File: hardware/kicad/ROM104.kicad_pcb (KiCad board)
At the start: 2 copper layers, 75 x 75 mm, 30 parts, among them J1 Screw_Terminal_01x12, J2 CAN, K1 DIPxx-1Cxx-51x, K2 DIPxx-1Cxx-51x, K3 DIPxx-1Cxx-51x, K4 DIPxx-1Cxx-51x, SW1 INSTANCE, SW2 BUS, U1 L293D, U2 MCP2551-I-P, U3 TMR_2411, U4 Teensy_3.2, U5 L293D

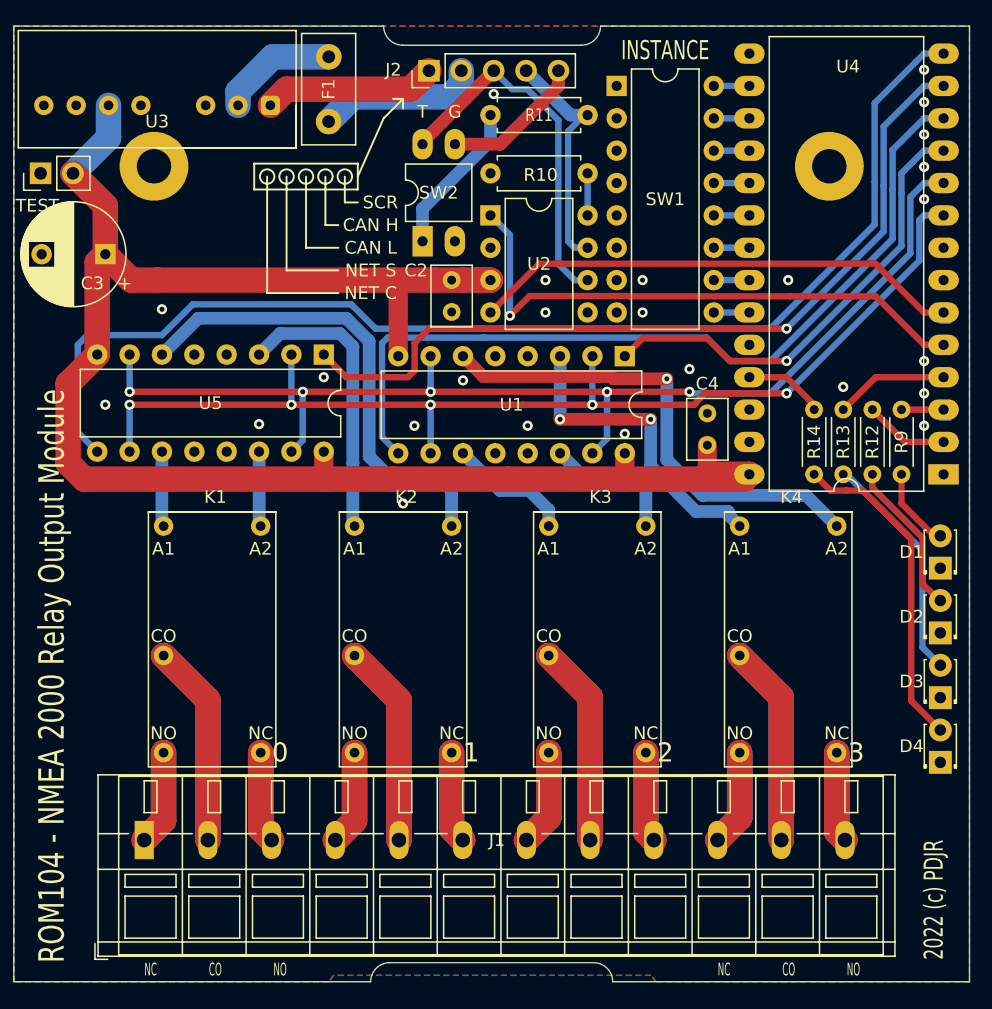
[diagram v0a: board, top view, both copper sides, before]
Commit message: Change relay terminal
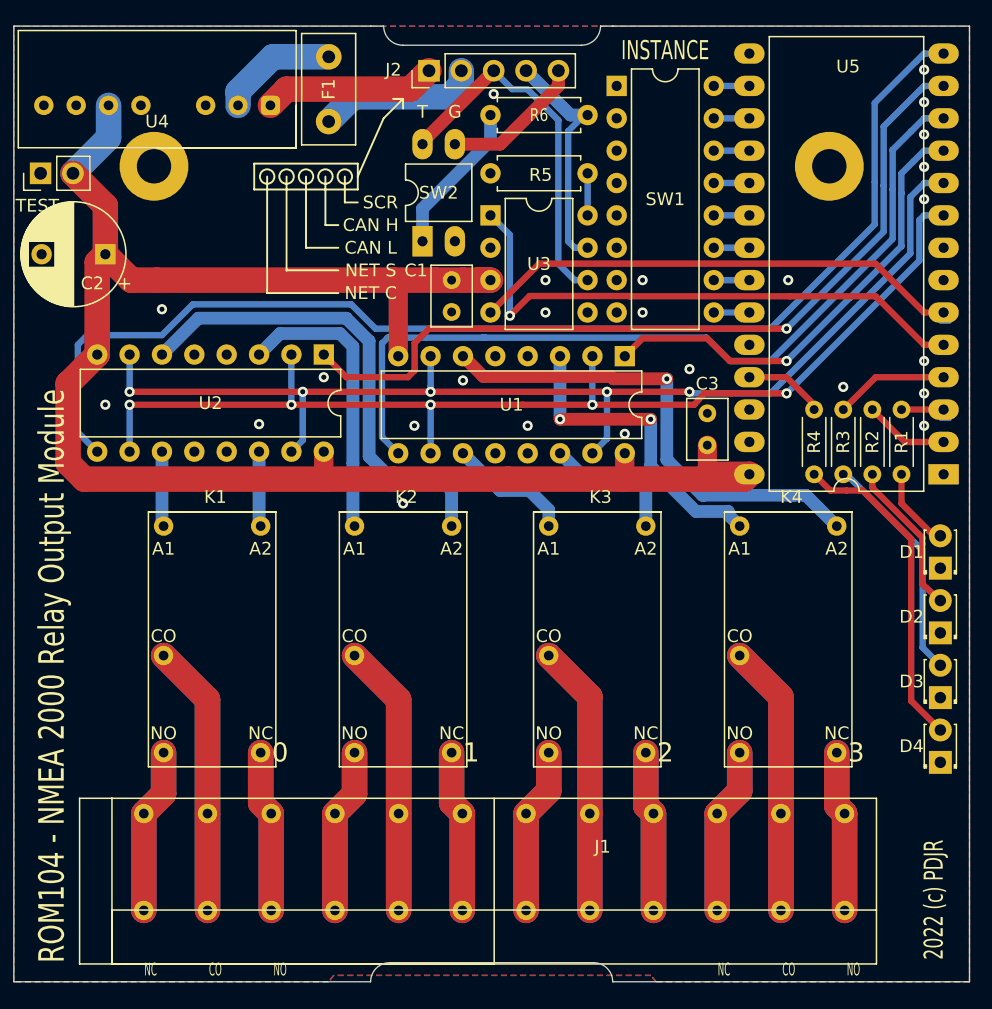
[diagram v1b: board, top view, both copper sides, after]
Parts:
- J1: footprint TerminalBlock_WAGO:TerminalBlock_WAGO_236-112_1x12_P5.00mm_45Degree -> PDJR-connectors:WURTH-401B-12PIN
- moved J1 5.52 mm to (146.2, 156.4)
- renumbered C2 to C1, C3 to C2, C4 to C3, R9 to R1, R12 to R2, R13 to R3, R14 to R4, R10 to R5, R11 to R6, U5 to U2, U2 to U3, U3 to U4, U4 to U5
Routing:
- net Net-(J1-Pad10): track 15.2 -> 26.2 mm
- net Net-(J1-Pad7): track 15.2 -> 26.2 mm
- net Net-(J1-Pad4): track 15.0 -> 26.0 mm
- net Net-(J1-Pad1): track 15.0 -> 26.0 mm
- net Net-(J1-Pad11): track 31.7 -> 42.7 mm
- net Net-(J1-Pad9): track 14.2 -> 25.3 mm
- net Net-(J1-Pad12): track 14.2 -> 25.3 mm
- net Net-(J1-Pad6): track 14.4 -> 25.5 mm
- net Net-(J1-Pad3): track 14.4 -> 25.4 mm
- net Net-(J1-Pad8): track 31.6 -> 42.7 mm
- net Net-(J1-Pad5): track 31.8 -> 42.9 mm
- net Net-(J1-Pad2): track 31.8 -> 42.9 mm

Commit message: PCB tweak
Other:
- board text removed: "0"
- board text removed: "1"
- board text removed: "2"
- board text removed: "3"
- board text removed: "CAN H"
- board text removed: "CAN L"
- board text removed: "NET C"
- board text removed: "NET S"
- board text removed: "SCR"

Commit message: Change resistor footprints
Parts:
- R5: footprint Resistor_THT:R_Axial_DIN0207_L6.3mm_D2.5mm_P7.62mm_Horizontal -> Resistor_THT:R_Axial_DIN0204_L3.6mm_D1.6mm_P5.08mm_Horizontal
- moved D1 4.07 mm to (209.0, 125.5), turned to 270 degrees
- moved D2 4.07 mm to (209.0, 130.6), turned to 270 degrees
- moved D3 4.07 mm to (209.0, 135.6), turned to 270 degrees
- moved D4 4.07 mm to (209.0, 140.7), turned to 270 degrees
- moved R5 2.59 mm to (175.9, 99.1)
- moved R4 1.27 mm to (197.5, 117.1)
- moved R3 1.02 mm to (200.1, 117.1)
- moved R2 0.76 mm to (202.6, 117.1)
- moved R1 0.51 mm to (205.2, 117.1)
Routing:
- net Net-(D3-Pad2): track 18.3 -> 20.4 mm
- net Net-(D1-Pad2): track 6.39 -> 8.31 mm
- net Net-(D2-Pad2): track 12.2 -> 14.1 mm
- net Net-(D4-Pad2): track 25.7 -> 27.5 mm
- net /CH2_LED: track 8.93 -> 10.0 mm
- net /CAN_H: track 18.5 -> 17.8 mm
- net /CH1_LED: track 6.64 -> 7.30 mm
- net /CAN_L: track 28.9 -> 28.3 mm
- net Net-(R5-Pad2): track 3.30 -> 2.79 mm
- net GND: vias 25 -> 26

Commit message: Update PCB
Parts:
- removed R1, R2, R3, R4: 470R, Resistor_THT:R_Axial_DIN0204_L3.6mm_D1.6mm_P5.08mm_Horizontal
- added RN1: 470R, Resistor_THT:R_Array_SIP5, F.Cu at (209.0, 146.3)
- K1, K2, K3, K4: value DIPxx-1Cxx-51x -> SPDT_RELAY
- R5: footprint Resistor_THT:R_Axial_DIN0204_L3.6mm_D1.6mm_P5.08mm_Horizontal -> Resistor_THT:R_Axial_DIN0207_L6.3mm_D2.5mm_P7.62mm_Horizontal
- moved R5 2.59 mm to (173.4, 98.6)
- moved D1 2.54 mm to (209.0, 128.0), turned to 90 degrees
- moved D2 2.54 mm to (209.0, 133.1), turned to 90 degrees
- moved D3 2.54 mm to (209.0, 138.2), turned to 90 degrees
- moved D4 2.54 mm to (209.0, 143.3), turned to 90 degrees
- moved K4 2.38 mm to (192.3, 146.3)
- moved K3 2.35 mm to (177.4, 146.3)
- moved K1 2.33 mm to (147.3, 146.3)
- moved K2 2.31 mm to (162.4, 146.3)
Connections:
- D1 pad 1: GND -> Net-(D1-Pad1)
- D1 pad 2: Net-(D1-Pad2) -> /CH0_LED
- D2 pad 1: GND -> Net-(D2-Pad1)
- D2 pad 2: Net-(D2-Pad2) -> /CH1_LED
- D3 pad 1: GND -> Net-(D3-Pad1)
- D3 pad 2: Net-(D3-Pad2) -> /CH2_LED
- D4 pad 1: GND -> Net-(D4-Pad1)
- D4 pad 2: Net-(D4-Pad2) -> /CH3_LED
- U5 pad 2: /CH1_LED -> /CH0_LED
- U5 pad 3: /CH0_LED -> /CH1_LED
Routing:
- net /CH3_LED: track 6.46 -> 38.0 mm
- net Net-(D1-Pad1): track 0.00 -> 31.2 mm
- net Net-(D4-Pad2): track 27.5 -> 0.00 mm
- net Net-(D2-Pad1): track 0.00 -> 23.0 mm
- net Net-(D3-Pad2): track 20.4 -> 0.00 mm
- net Net-(D3-Pad1): track 0.00 -> 14.8 mm
- net Net-(D2-Pad2): track 14.1 -> 0.00 mm
- net /CH2_LED: track 10.0 -> 23.6 mm
- net Net-(D1-Pad2): track 8.31 -> 0.00 mm
- net /CH1_LED: track 7.30 -> 15.4 mm
- net Net-(D4-Pad1): track 0.00 -> 6.64 mm
- net Net-(J1-Pad7): track 26.2 -> 21.3 mm
- net Net-(J1-Pad10): track 26.2 -> 21.3 mm
- net Net-(J1-Pad1): track 26.0 -> 21.2 mm
- net Net-(J1-Pad4): track 26.0 -> 21.3 mm
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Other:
- board text removed: "CO"
- board text removed: "NC"
- board text removed: "NO"

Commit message: PCB tweak
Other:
- board text added: "CHANNEL 0"
- board text added: "CHANNEL 1"
- board text added: "CHANNEL 2"
- board text added: "CHANNEL 3"

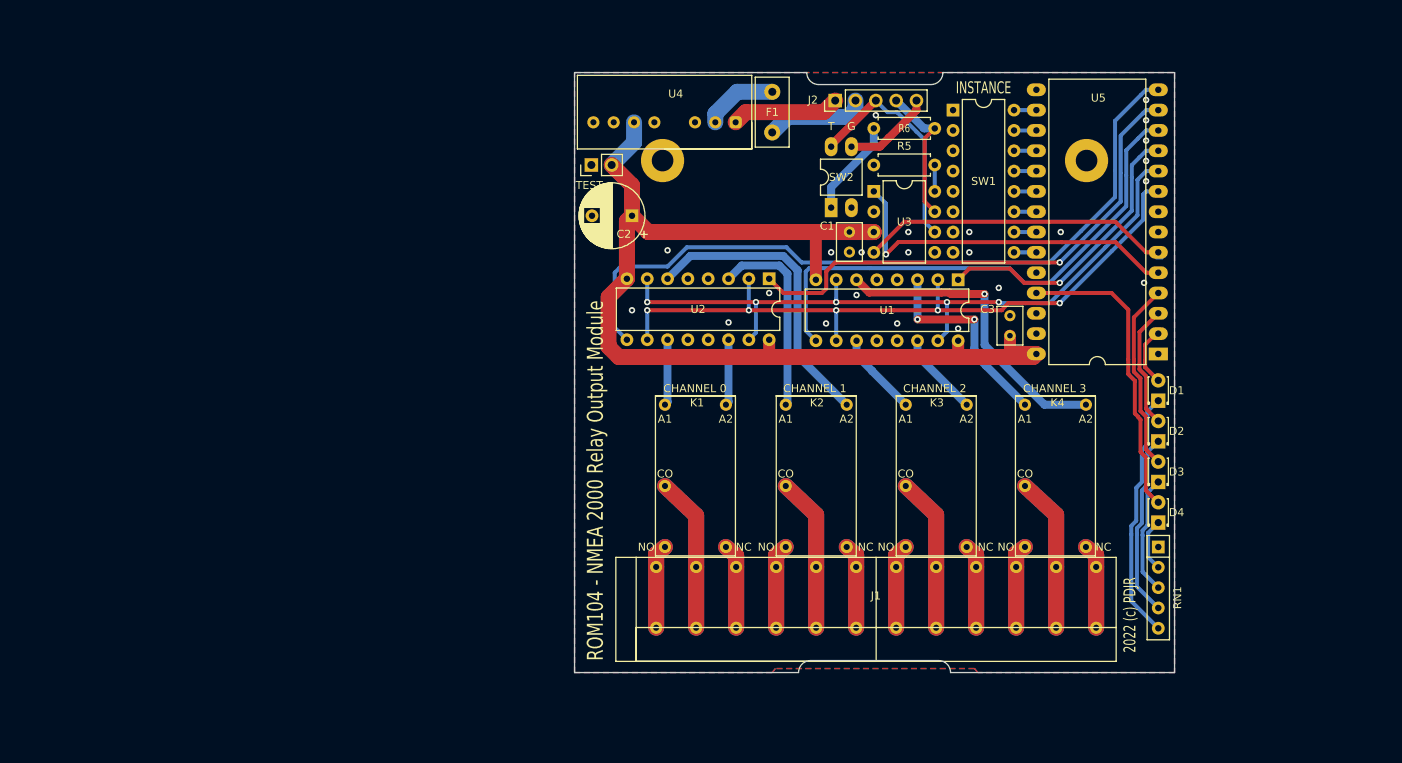
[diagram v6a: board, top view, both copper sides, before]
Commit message: PCB resize
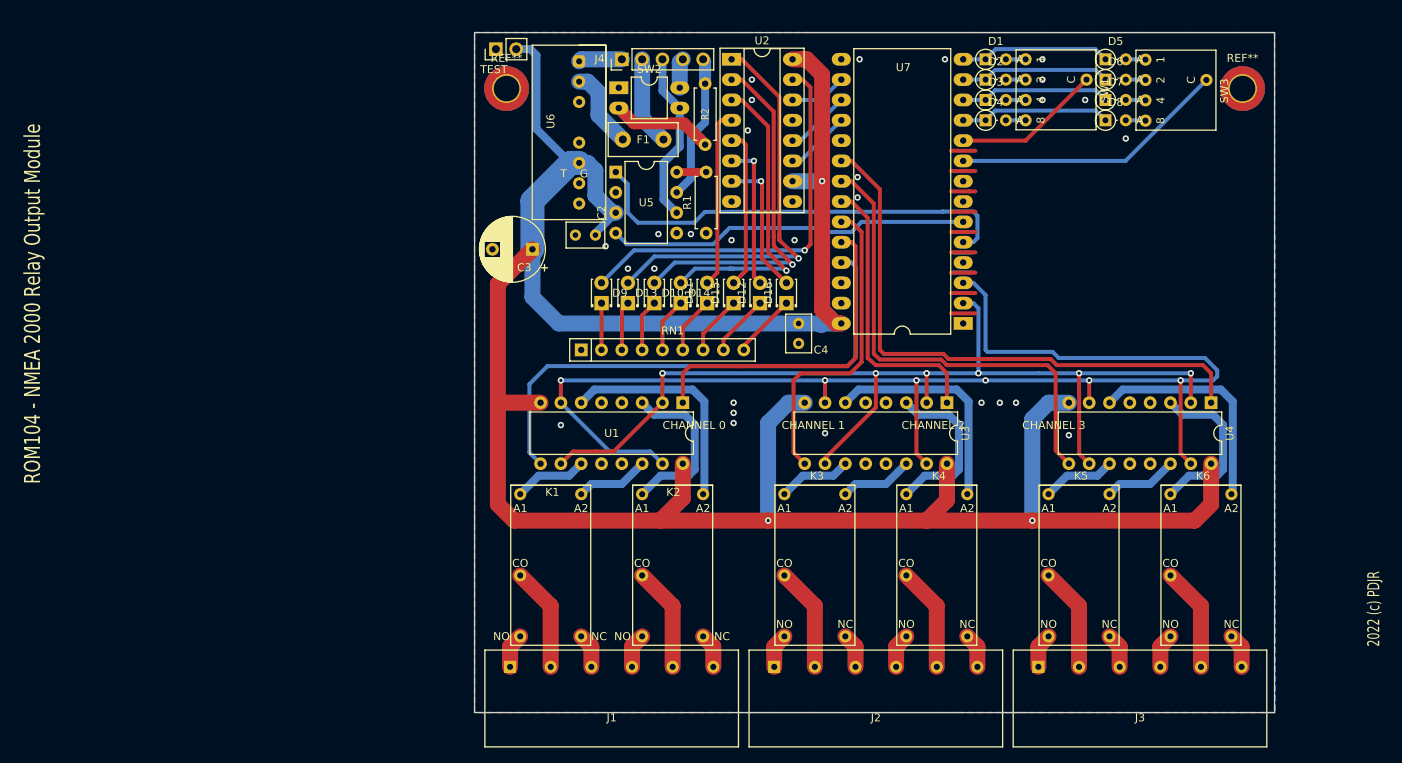
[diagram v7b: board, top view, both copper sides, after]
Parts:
- removed C1: 100n, Capacitor_THT:C_Rect_L4.6mm_W3.0mm_P2.50mm_MKS02_FKP02
- removed R5: 4K7, Resistor_THT:R_Axial_DIN0207_L6.3mm_D2.5mm_P7.62mm_Horizontal
- removed R6: 120R, Resistor_THT:R_Axial_DIN0207_L6.3mm_D2.5mm_P7.62mm_Horizontal
- removed the REF** at (200.0, 98.0)
- removed the REF** at (147.0, 98.0)
- removed the U1 at (183.9, 112.9)
- added C2: 100n, Capacitor_THT:C_Rect_L4.6mm_W3.0mm_P2.50mm_MKS02_FKP02, F.Cu at (138.6, 107.3)
- added D11: LED, LED_THT:LED_D1.8mm_W3.3mm_H2.4mm, F.Cu at (152.6, 115.8)
- added D12: LED, LED_THT:LED_D1.8mm_W3.3mm_H2.4mm, F.Cu at (159.2, 115.8)
- added D13: LED, LED_THT:LED_D1.8mm_W3.3mm_H2.4mm, F.Cu at (142.7, 115.8)
- added D15: LED, LED_THT:LED_D1.8mm_W3.3mm_H2.4mm, F.Cu at (155.9, 115.8)
- added D16: LED, LED_THT:LED_D1.8mm_W3.3mm_H2.4mm, F.Cu at (162.5, 115.8)
- added D3: D_Small, Diode_THT:D_DO-34_SOD68_P2.54mm_Vertical_AnodeUp, F.Cu at (187.4, 90.4)
- added D4: D_Small, Diode_THT:D_DO-34_SOD68_P2.54mm_Vertical_AnodeUp, F.Cu at (187.4, 93.0)
- added D5: D_Small, Diode_THT:D_DO-34_SOD68_P2.54mm_Vertical_AnodeUp, F.Cu at (202.4, 85.3)
- added D6: D_Small, Diode_THT:D_DO-34_SOD68_P2.54mm_Vertical_AnodeUp, F.Cu at (202.4, 87.9)
- added D7: D_Small, Diode_THT:D_DO-34_SOD68_P2.54mm_Vertical_AnodeUp, F.Cu at (202.4, 90.4)
- added D8: D_Small, Diode_THT:D_DO-34_SOD68_P2.54mm_Vertical_AnodeUp, F.Cu at (202.4, 93.0)
- added D9: LED, LED_THT:LED_D1.8mm_W3.3mm_H2.4mm, F.Cu at (139.4, 115.8)
- added J3: Screw_Terminal_01x06, PDJR-connectors:879-1272_TERMINAL_HEADER_6-POLE, F.Cu at (219.4, 161.3)
- added J4: CAN, Connector_PinHeader_2.54mm:PinHeader_1x05_P2.54mm_Vertical, F.Cu at (141.9, 85.3)
- added K5: SPDT_RELAY, PDJR-connectors:PE014F05, F.Cu at (195.2, 157.5)
- added K6: SPDT_RELAY, PDJR-connectors:PE014F05, F.Cu at (210.5, 157.5)
- added R1: 4K7, Resistor_THT:R_Axial_DIN0207_L6.3mm_D2.5mm_P7.62mm_Horizontal, F.Cu at (152.5, 107.1)
- added R2: 120R, Resistor_THT:R_Axial_DIN0207_L6.3mm_D2.5mm_P7.62mm_Horizontal, F.Cu at (152.3, 88.4)
- added REF**: MountingHole_3.2mm_M3_DIN965_Pad_TopBottom, MountingHole:MountingHole_3.2mm_M3_DIN965_Pad_TopBottom, F.Cu at (127.5, 89.0)
- added REF**: MountingHole_3.2mm_M3_DIN965_Pad_TopBottom, MountingHole:MountingHole_3.2mm_M3_DIN965_Pad_TopBottom, F.Cu at (219.5, 89.0)
- added SW3: HEX_ENCODER, PDJR-connectors:FR01-SR16P-ST, F.Cu at (206.2, 84.2)
- added U2: 74HC595, Package_DIP:DIP-16_W7.62mm_Socket_LongPads, F.Cu at (155.6, 85.3)
- added U4: L293D, Package_DIP:DIP-16_W7.62mm, F.Cu at (215.6, 128.3)
- added U5: MCP2551-I-P, Package_DIP:DIP-8_W7.62mm, F.Cu at (141.1, 99.4)
- D1, D2: value LED -> D_Small; footprint LED_THT:LED_D1.8mm_W3.3mm_H2.4mm -> Diode_THT:D_DO-34_SOD68_P2.54mm_Vertical_AnodeUp
- J1: value Screw_Terminal_01x12 -> Screw_Terminal_01x06; footprint PDJR-connectors:WURTH-401B-12PIN -> PDJR-connectors:879-1272_TERMINAL_HEADER_6-POLE
- J2: value CAN -> Screw_Terminal_01x06; footprint Connector_PinHeader_2.54mm:PinHeader_1x05_P2.54mm_Vertical -> PDJR-connectors:879-1272_TERMINAL_HEADER_6-POLE
- RN1: value 470R -> R_Network08; footprint Resistor_THT:R_Array_SIP5 -> Resistor_THT:R_Array_SIP9
- SW1: value INSTANCE -> HEX_ENCODER; footprint Package_DIP:DIP-16_W7.62mm -> PDJR-connectors:FR01-SR16P-ST
- U3: value MCP2551-I-P -> L293D; footprint Package_DIP:DIP-8_W7.62mm -> Package_DIP:DIP-16_W7.62mm
- moved RN1 76.2 mm to (136.8, 121.7), turned to 0 degrees
- moved J2 73.0 mm to (186.4, 161.3), turned to 180 degrees
- moved D10 66.8 mm to (146.0, 115.8)
- moved D14 65.7 mm to (149.3, 115.8)
- moved D2 50.1 mm to (187.4, 87.9), turned to 0 degrees
- moved D1 47.8 mm to (187.4, 85.3), turned to 0 degrees
- moved SW2 30.5 mm to (141.5, 88.9), turned to 0 degrees
- moved U3 28.0 mm to (182.6, 128.3), turned to 270 degrees
- moved C4 26.5 mm to (164.0, 118.4), turned to 270 degrees
- moved U7 24.7 mm to (184.6, 118.4)
- moved K1 21.3 mm to (129.2, 157.5)
- moved K2 21.1 mm to (144.4, 157.5)
- moved U6 21.0 mm to (136.6, 85.6), turned to 270 degrees
- moved U1 18.9 mm to (149.5, 128.3)
- moved K3 18.8 mm to (162.2, 157.5)
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- renumbered C2 to C3, C3 to C4, D3 to D10, D4 to D14, U2 to U1, U4 to U6, U5 to U7
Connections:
- D1 pad 1: Net-(D1-Pad1) -> /ADDR_0
- D1 pad 2: /CH0_LED -> Net-(D1-Pad2)
- D10 pad 1: Net-(D3-Pad1) -> Net-(D10-Pad1)
- D10 pad 2: /CH2_LED -> Net-(D10-Pad2)
- D14 pad 1: Net-(D4-Pad1) -> Net-(D14-Pad1)
- D14 pad 2: /CH3_LED -> Net-(D14-Pad2)
- D2 pad 1: Net-(D2-Pad1) -> /ADDR_1
- D2 pad 2: /CH1_LED -> Net-(D2-Pad2)
- J2 pad 1: /NET_C -> Net-(J2-Pad1)
- J2 pad 2: Net-(F1-Pad1) -> Net-(J2-Pad2)
- J2 pad 3: /CAN_L -> Net-(J2-Pad3)
- J2 pad 4: /CAN_H -> Net-(J2-Pad4)
- J2 pad 5: /CAN_SCR -> Net-(J2-Pad5)
- K3 pad 1: Net-(J1-Pad9) -> Net-(J2-Pad3)
- K3 pad 14: Net-(J1-Pad7) -> Net-(J2-Pad1)
- K3 pad 7: Net-(J1-Pad8) -> Net-(J2-Pad2)
- K4 pad 1: Net-(J1-Pad12) -> Net-(J2-Pad6)
- K4 pad 14: Net-(J1-Pad10) -> Net-(J2-Pad4)
- K4 pad 7: Net-(J1-Pad11) -> Net-(J2-Pad5)
- RN1 pad 2: Net-(D4-Pad1) -> Net-(D9-Pad1)
- RN1 pad 3: Net-(D3-Pad1) -> Net-(D13-Pad1)
- RN1 pad 4: Net-(D2-Pad1) -> Net-(D10-Pad1)
- RN1 pad 5: Net-(D1-Pad1) -> Net-(D14-Pad1)
- SW1 pad 1: GND -> Net-(D1-Pad2)
- SW1 pad 2: GND -> Net-(D2-Pad2)
- SW1 pad 3: GND -> Net-(D3-Pad2)
- SW1 pad 4: GND -> Net-(D4-Pad2)
- SW1 pad 5: GND -> /ADDR_HI
- SW2 pad 1: /TERM_A -> GND
- SW2 pad 2: GND -> /TERM_A
- SW2 pad 3: /CAN_SCR -> /CAN_L
- SW2 pad 4: /CAN_L -> /CAN_SCR
- U3 pad 1: /CAN_TX -> /CH3_EN
- U3 pad 2: GND -> /RST
- U3 pad 3: +5V -> Net-(K4-Pad6)
- U3 pad 4: /CAN_RX -> GND
- U3 pad 5: Net-(U3-Pad5) -> GND
- U3 pad 6: /CAN_L -> Net-(K4-Pad2)
- U3 pad 7: /CAN_H -> /SET
- U3 pad 8: Net-(R5-Pad2) -> +5V
- U7 pad 10: /SET -> /ADDR_HI
- U7 pad 11: /CH3_EN -> /ADDR_3
- U7 pad 12: /CH2_EN -> /ADDR_2
- U7 pad 13: /CH1_EN -> /ADDR_1
- U7 pad 14: /CH0_EN -> /ADDR_0
- U7 pad 16: /ADDR_0 -> /MPX_DATA
- U7 pad 17: /ADDR_1 -> /MPX_LATCH
- U7 pad 18: /ADDR_2 -> /MPX_CLOCK
- U7 pad 19: /ADDR_3 -> Net-(U7-Pad19)
- U7 pad 2: /CH0_LED -> /RST
- U7 pad 20: /ADDR_4 -> /CH5_EN
- U7 pad 21: /ADDR_5 -> /CH4_EN
- U7 pad 22: /ADDR_6 -> /CH3_EN
- U7 pad 23: /ADDR_7 -> /CH2_EN
- U7 pad 24: Net-(U5-Pad24) -> /CH1_EN
- U7 pad 25: /CH3_LED -> /CH0_EN
- U7 pad 3: /CH1_LED -> /SET
- U7 pad 4: /CH2_LED -> Net-(U7-Pad4)
- U7 pad 9: /RST -> /ADDR_LO
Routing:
- net +5V: track 134.6 -> 319.1 mm, vias 0 -> 3
- net /SET: track 89.4 -> 169.4 mm, vias 5 -> 6
- net /CH5_EN: track 0.00 -> 72.7 mm
- net /CH4_EN: track 0.00 -> 59.7 mm
- net Net-(D13-Pad2): track 0.00 -> 52.3 mm, vias 0 -> 1
- net Net-(D9-Pad2): track 0.00 -> 50.4 mm, vias 0 -> 1
- net Net-(D10-Pad2): track 0.00 -> 45.4 mm, vias 0 -> 1
- net /RST: track 87.2 -> 129.1 mm, vias 5 -> 6
- net Net-(D14-Pad2): track 0.00 -> 39.5 mm, vias 0 -> 1
- net Net-(J1-Pad11): track 38.9 -> 0.00 mm
- net Net-(J1-Pad8): track 38.7 -> 0.00 mm
- net /CH3_LED: track 38.0 -> 0.00 mm
- net /ADDR_LO: track 0.00 -> 34.6 mm
- net Net-(D1-Pad1): track 31.2 -> 0.00 mm
- net GND: track 0.00 -> 29.5 mm, vias 23 -> 28
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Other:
- board size 75 x 75 mm -> 100 x 85 mm

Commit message: New PCB layout
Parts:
- removed the D1 at (187.4, 85.3)
- removed the D2 at (187.4, 87.9)
- removed the D3 at (187.4, 90.4)
- removed the D4 at (187.4, 93.0)
- removed the D5 at (202.4, 85.3)
- removed the D6 at (202.4, 87.9)
- removed the D7 at (202.4, 90.4)
- removed the D8 at (202.4, 93.0)
- removed SW3: HEX_ENCODER, PDJR-connectors:FR01-SR16P-ST
- removed the U2 at (155.6, 85.3)
- added C1: 100n, Capacitor_THT:C_Rect_L4.6mm_W3.0mm_P2.50mm_MKS02_FKP02, F.Cu at (195.4, 102.9)
- added U3: 74HC595, Package_DIP:DIP-16_W7.62mm_Socket_LongPads, F.Cu at (198.8, 108.1)
- SW1: value HEX_ENCODER -> INSTANCE; footprint PDJR-connectors:FR01-SR16P-ST -> Package_DIP:DIP-16_W7.62mm
- moved RN1 61.6 mm to (198.3, 118.2)
- moved D2 56.1 mm to (202.1, 115.2)
- moved D4 56.1 mm to (215.3, 115.2)
- moved D5 56.1 mm to (198.8, 115.2)
- moved D7 56.1 mm to (212.0, 115.2)
- moved D1 56.1 mm to (195.5, 115.2)
- moved D3 56.1 mm to (208.7, 115.2)
- moved D6 56.1 mm to (205.4, 115.2)
- moved D8 56.1 mm to (218.6, 115.2)
- moved C3 40.4 mm to (162.2, 83.8), turned to 270 degrees
- moved R2 24.4 mm to (134.0, 104.5), turned to 90 degrees
- moved J4 16.9 mm to (127.6, 94.4), turned to 0 degrees
- moved F1 15.4 mm to (133.0, 89.3), turned to 90 degrees
- moved SW1 10.8 mm to (195.8, 94.0), turned to 90 degrees
- moved C4 7.31 mm to (171.2, 119.4), turned to 90 degrees
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- renumbered D9 to D1, D10 to D2, D11 to D3, D12 to D4, D13 to D5, D14 to D6, D15 to D7, D16 to D8, U3 to U2
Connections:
- net /ADDR_HI renamed /ADDR_4
- SW1 pad 1: Net-(D1-Pad2) (its old number) -> /ADDR_0
- SW1 pad 2: Net-(D2-Pad2) (its old number) -> /ADDR_1
- SW1 pad 3: Net-(D3-Pad2) (its old number) -> /ADDR_2
- SW1 pad 4: Net-(D4-Pad2) (its old number) -> /ADDR_3
- U7 pad 16: /MPX_DATA -> Net-(U7-Pad16)
- U7 pad 17: /MPX_LATCH -> Net-(U7-Pad17)
- U7 pad 18: /MPX_CLOCK -> /CH5_EN
- U7 pad 19: Net-(U7-Pad19) -> /CH4_EN
- U7 pad 2: /RST -> /MPX_CLOCK
- U7 pad 20: /CH5_EN -> /CH3_EN
- U7 pad 21: /CH4_EN -> /CH2_EN
- U7 pad 22: /CH3_EN -> /CH1_EN
- U7 pad 23: /CH2_EN -> /CH0_EN
- U7 pad 24: /CH1_EN -> /SET
- U7 pad 25: /CH0_EN -> /RST
- U7 pad 3: /SET -> /MPX_LATCH
- U7 pad 4: Net-(U7-Pad4) -> /MPX_DATA
- U7 pad 7: Net-(U7-Pad7) -> /ADDR_7
- U7 pad 8: Net-(U7-Pad8) -> /ADDR_6
- U7 pad 9: /ADDR_LO -> /ADDR_5
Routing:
- net +5V: track 319.1 -> 524.5 mm, vias 3 -> 2
- net Net-(D5-Pad2): track 52.3 -> 4.57 mm, vias 1 -> 0
- net Net-(D2-Pad2): track 45.4 -> 4.89 mm, vias 1 -> 0
- net Net-(D1-Pad2): track 50.4 -> 14.6 mm, vias 1 -> 0
- net /ADDR_LO: track 34.6 -> 0.00 mm
- net Net-(D6-Pad2): track 39.5 -> 5.20 mm, vias 1 -> 0
- net /SET: track 169.4 -> 202.1 mm, vias 6 -> 8
- net /CAN_SCR: track 3.71 -> 34.3 mm
- net /ADDR_7: track 0.00 -> 28.5 mm
- net GND: track 29.5 -> 4.72 mm, vias 28 -> 30
- net /ADDR_6: track 0.00 -> 23.9 mm
- net /MPX_CLOCK: track 8.20 -> 30.9 mm
- net /ADDR_5: track 0.00 -> 19.4 mm
- net /MPX_LATCH: track 8.20 -> 26.0 mm
- net Net-(D3-Pad2): track 22.3 -> 5.52 mm
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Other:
- board text added: "1"
- board text added: "128"
- board text added: "16"
- board text added: "2"
- board text added: "32"
- board text added: "4"
- board text added: "64"
- board text added: "8"
- board text added: "CHANNEL 4"
- board text added: "CHANNEL 5"
